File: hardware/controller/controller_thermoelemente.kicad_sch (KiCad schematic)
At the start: 15 parts, among them J5 TC top, J6 TC bot, U5 MAX31856MUD+, U6 MAX31856MUD+

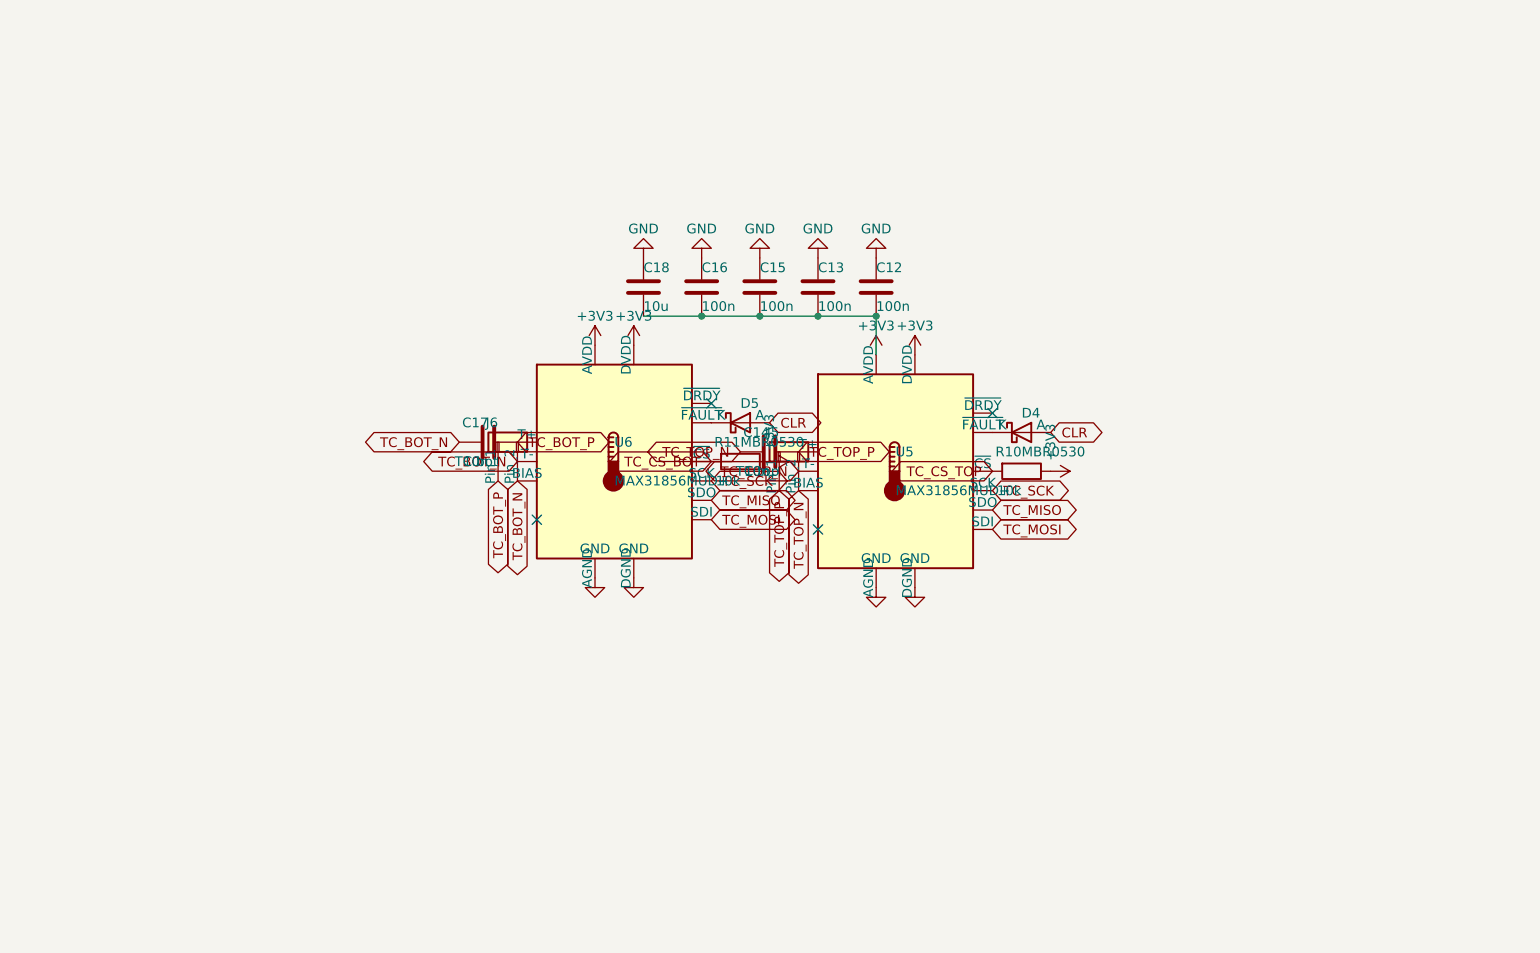
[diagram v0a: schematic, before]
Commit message: feat(hardware): MAX31856 input filter per datasheet, sheet cleanup in progress
- Input filter per MAX31856 "Typical Application Circuit": C14/C17 100 nF
  differential, new C27-C30 10 nF from T+/T- to GND; reference netlist re-exported
- Datasheet checks: BIAS to T- confirmed, FAULT is push-pull (diodes to CLR needed)
- check_schematic.py: sheet format check (raw newline in strings breaks KiCad)
- import_netlist.py: relinks by reference when a symbol gets a new UUID (U7 case)
- Sheets partly rearranged in KiCad by the user (connectivity unchanged, 0 errors)
- MAX31856 order number and price, docs/Component-Specs ignored

Co-Authored-By: Claude Opus 5.5 <noreply@anthropic.com>
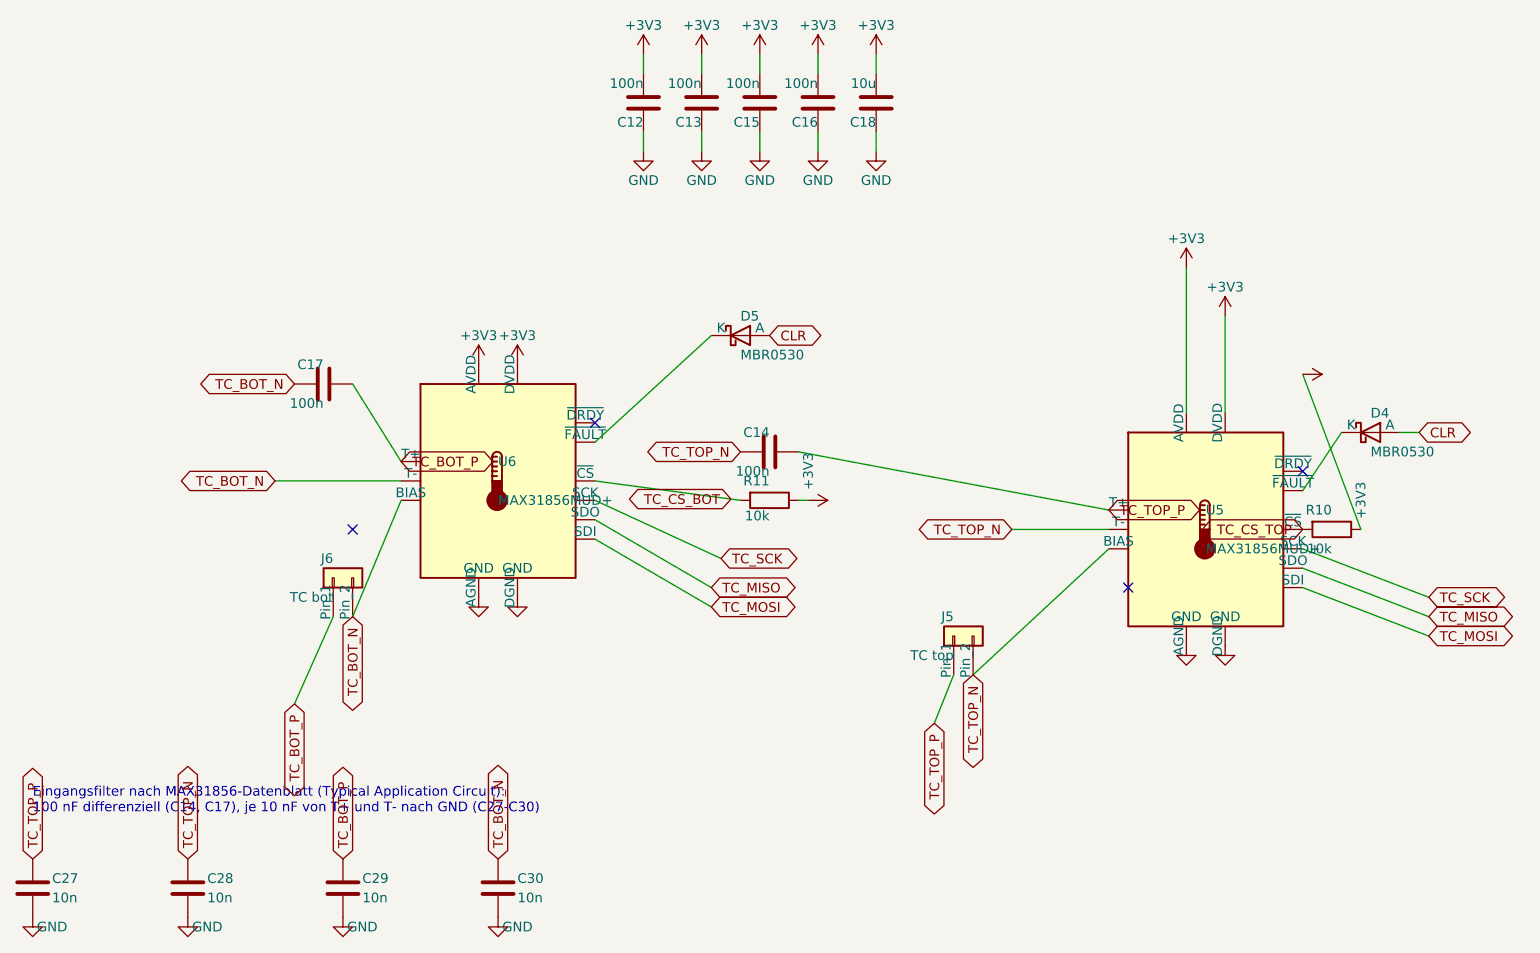
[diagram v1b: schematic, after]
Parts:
- added C27, C28, C29, C30: 10n, Capacitor_SMD:C_0603_1608Metric, symbol Device:C
- C14, C17: value 10n -> 100n
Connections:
- net GND: now also C27.2, C28.2, C29.2, C30.2
- net TC_BOT_N: now also C30.1
- net TC_BOT_P: now also C29.1
- net TC_TOP_N: now also C28.1
- net TC_TOP_P: now also C27.1
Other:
- note added: "Eingangsfilter nach MAX31856-Datenblatt (Typical Application Circuit): 100 nF differenziell (C14, C17), je 10 nF von T+ und T- nach GND (C27-C30)"
- moved on the sheet: C12, C13, C15, C16, C17, C18, D4, D5, J5, J6, R10, R11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
